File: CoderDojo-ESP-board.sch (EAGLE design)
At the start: 37 parts, among them IC1 ESP-12E/F, IC2 FT232RL, U1 PCA9685PW,118, U2 AMS1117-3.3, X1 PN61729-S

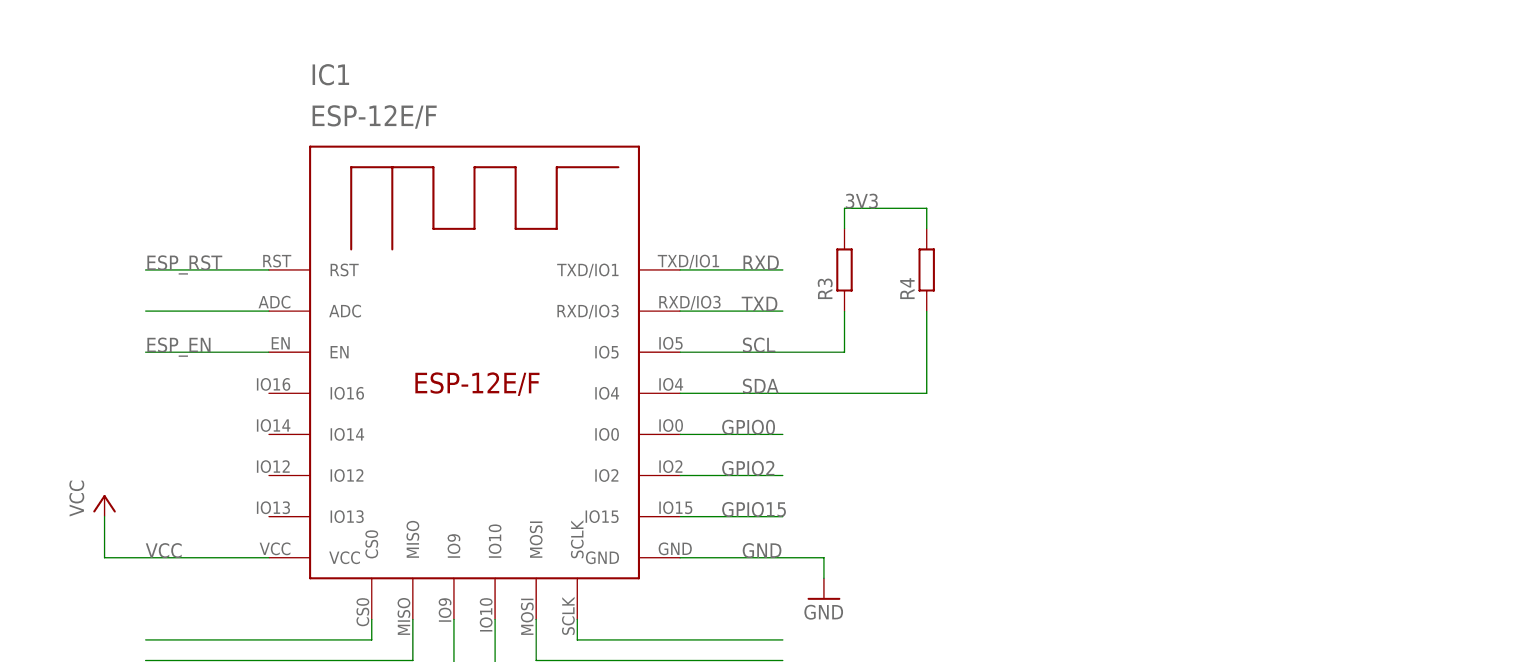
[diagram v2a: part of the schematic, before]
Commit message: add gitignore + add display to schematic
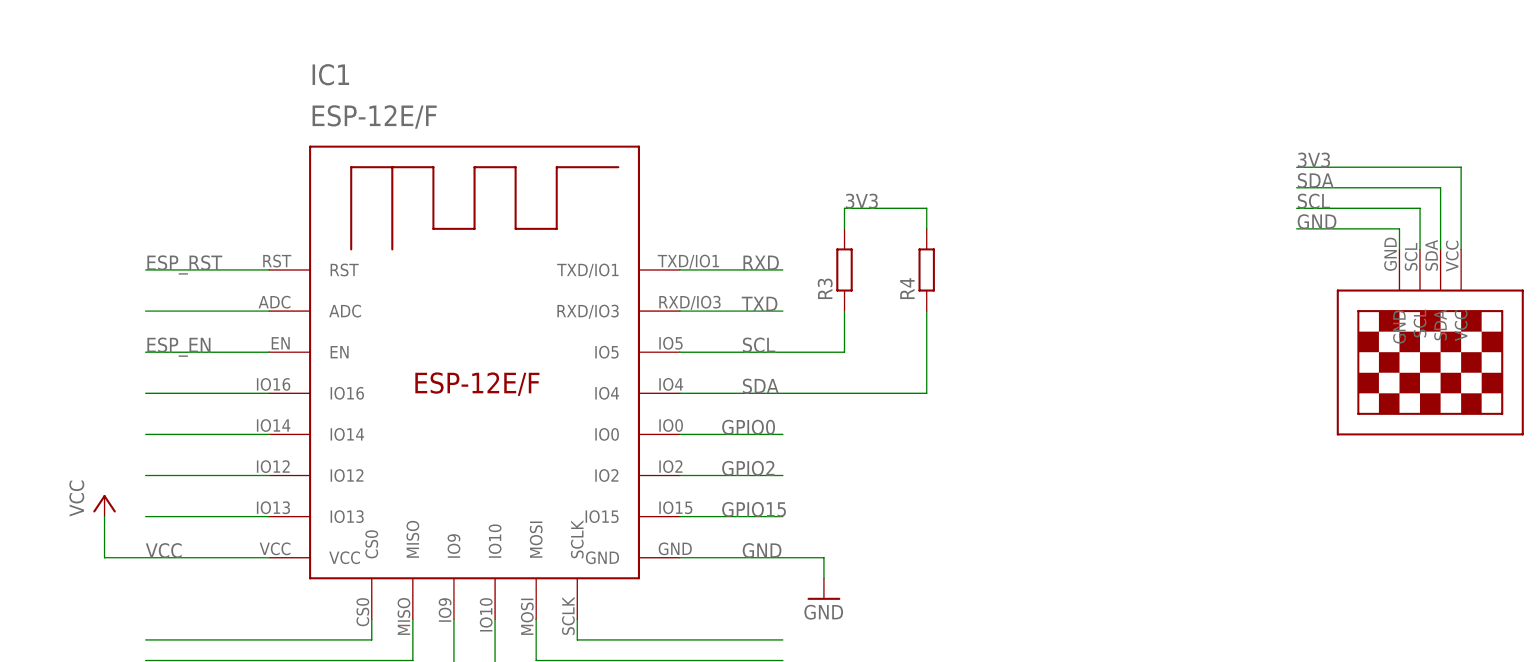
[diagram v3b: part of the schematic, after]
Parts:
- added U$1: 13"OLED13"OLED, 13oled:13"OLED13"OLED
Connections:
- new net N$4: IC1.IO16
- new net N$5: IC1.IO14
- new net N$6: IC1.IO12
- new net N$7: IC1.IO13
- net 3V3: now also U$1.VCC
- net GND: now also U$1.GND
- net SCL: now also U$1.SCL
- net SDA: now also U$1.SDA
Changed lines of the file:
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@@
 <layer number="97" name="Info" color="7" fill="1" visible="yes" active="yes"/>
 <layer number="98" name="Guide" color="6" fill="1" visible="yes" active="yes"/>
+<layer number="101" name="Hidden" color="15" fill="1" visible="yes" active="yes"/>
+<layer number="102" name="Changes" color="12" fill="1" visible="yes" active="yes"/>
 </layers>
 <schematic xreflabel="%F%N/%S.%C%R" xrefpart="/%S.%C%R">
@@
 <part name="C3" library="rcl" library_urn="urn:adsk.eagle:library:334" deviceset="C-EU" device="C0805" package3d_urn="urn:adsk.eagle:package:23617/2"/>
 <part name="C4" library="rcl" library_urn="urn:adsk.eagle:library:334" deviceset="C-EU" device="C0805" package3d_urn="urn:adsk.eagle:package:23617/2"/>
+<part name="U$1" library="13oled" deviceset="13&quot;OLED" device="13&quot;OLED"/>
 </parts>
 <sheets>
@@
 <attribute name="VALUE" x="98.044" y="129.921" size="1.778" layer="96"/>
 </instance>
+<instance part="U$1" gate="G$1" x="314.96" y="71.12" smashed="yes"/>
 </instances>
 <busses>
@@
 <label x="132.08" y="185.42" size="1.778" layer="95"/>
 </segment>
+<segment>
+<pinref part="U$1" gate="G$1" pin="GND"/>
+<wire x1="312.42" y1="83.82" x2="312.42" y2="86.36" width="0.1524" layer="91"/>
+<wire x1="312.42" y1="86.36" x2="299.72" y2="86.36" width="0.1524" layer="91"/>
+<label x="299.72" y="86.36" size="1.778" layer="95"/>
+</segment>
 </net>
 <net name="TXD" class="0">
@@
 <label x="185.42" y="185.42" size="1.778" layer="95"/>
 </segment>
+<segment>
+<pinref part="U$1" gate="G$1" pin="SDA"/>
+<wire x1="317.5" y1="83.82" x2="317.5" y2="91.44" width="0.1524" layer="91"/>
+<wire x1="317.5" y1="91.44" x2="299.72" y2="91.44" width="0.1524" layer="91"/>
+<label x="299.72" y="91.44" size="1.778" layer="95"/>
+</segment>
 </net>
 <net name="SCL" class="0">
@@
 <wire x1="144.78" y1="177.8" x2="132.08" y2="177.8" width="0.1524" layer="91"/>
 <label x="132.08" y="177.8" size="1.778" layer="95"/>
+</segment>
+<segment>
+<pinref part="U$1" gate="G$1" pin="SCL"/>
+<wire x1="314.96" y1="83.82" x2="314.96" y2="88.9" width="0.1524" layer="91"/>
+<wire x1="314.96" y1="88.9" x2="299.72" y2="88.9" width="0.1524" layer="91"/>
+<label x="299.72" y="88.9" size="1.778" layer="95"/>
 </segment>
 </net>
@@
 <label x="86.36" y="142.24" size="1.778" layer="95"/>
 </segment>
+<segment>
+<pinref part="U$1" gate="G$1" pin="VCC"/>
+<wire x1="320.04" y1="83.82" x2="320.04" y2="93.98" width="0.1524" layer="91"/>
+<wire x1="320.04" y1="93.98" x2="299.72" y2="93.98" width="0.1524" layer="91"/>
+<label x="299.72" y="93.98" size="1.778" layer="95"/>
+</segment>
 </net>
 <net name="3V3FT" class="0">
@@
 </segment>
 </net>
+<net name="N$4" class="0">
+<segment>
+<pinref part="IC1" gate="G$1" pin="IO16"/>
+<wire x1="172.72" y1="66.04" x2="157.48" y2="66.04" width="0.1524" layer="91"/>
+</segment>
+</net>
+<net name="N$5" class="0">
+<segment>
+<pinref part="IC1" gate="G$1" pin="IO14"/>
+<wire x1="172.72" y1="60.96" x2="157.48" y2="60.96" width="0.1524" layer="91"/>
+</segment>
+</net>
+<net name="N$6" class="0">
+<segment>
+<pinref part="IC1" gate="G$1" pin="IO12"/>
+<wire x1="172.72" y1="55.88" x2="157.48" y2="55.88" width="0.1524" layer="91"/>
+</segment>
+</net>
+<net name="N$7" class="0">
+<segment>
+<pinref part="IC1" gate="G$1" pin="IO13"/>
+<wire x1="172.72" y1="50.8" x2="157.48" y2="50.8" width="0.1524" layer="91"/>
+</segment>
+</net>

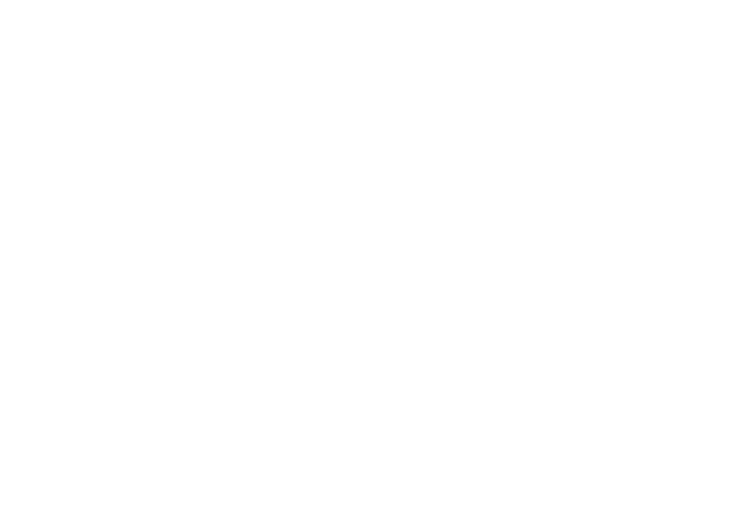
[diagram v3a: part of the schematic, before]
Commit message: Add User buttons
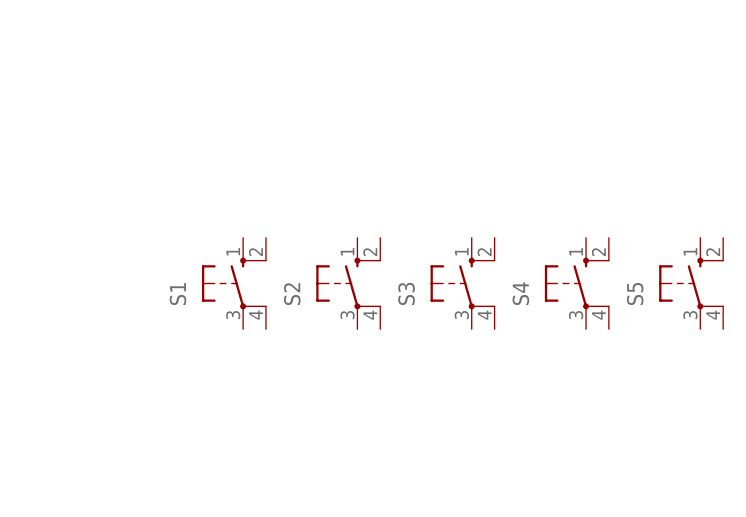
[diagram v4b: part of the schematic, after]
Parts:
- added S1, S2, S3, S4, S5: (no value), switch-omron:10-XX
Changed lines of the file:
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@@
 <part name="C4" library="rcl" library_urn="urn:adsk.eagle:library:334" deviceset="C-EU" device="C0805" package3d_urn="urn:adsk.eagle:package:23617/2"/>
 <part name="U$1" library="13oled" deviceset="13&quot;OLED" device="13&quot;OLED"/>
+<part name="S1" library="switch-omron" library_urn="urn:adsk.eagle:library:377" deviceset="10-XX" device="" package3d_urn="urn:adsk.eagle:package:27496/1"/>
+<part name="S2" library="switch-omron" library_urn="urn:adsk.eagle:library:377" deviceset="10-XX" device="" package3d_urn="urn:adsk.eagle:package:27496/1"/>
+<part name="S3" library="switch-omron" library_urn="urn:adsk.eagle:library:377" deviceset="10-XX" device="" package3d_urn="urn:adsk.eagle:package:27496/1"/>
+<part name="S4" library="switch-omron" library_urn="urn:adsk.eagle:library:377" deviceset="10-XX" device="" package3d_urn="urn:adsk.eagle:package:27496/1"/>
+<part name="S5" library="switch-omron" library_urn="urn:adsk.eagle:library:377" deviceset="10-XX" device="" package3d_urn="urn:adsk.eagle:package:27496/1"/>
 </parts>
 <sheets>
@@
 </instance>
 <instance part="U$1" gate="G$1" x="314.96" y="71.12" smashed="yes"/>
+<instance part="S1" gate="1" x="314.96" y="-7.62" smashed="yes">
+<attribute name="NAME" x="308.61" y="-10.16" size="1.778" layer="95" rot="R90"/>
+<attribute name="VALUE" x="311.15" y="-4.445" size="1.778" layer="96" rot="R90"/>
+</instance>
+<instance part="S2" gate="1" x="327.66" y="-7.62" smashed="yes">
+<attribute name="NAME" x="321.31" y="-10.16" size="1.778" layer="95" rot="R90"/>
+<attribute name="VALUE" x="323.85" y="-4.445" size="1.778" layer="96" rot="R90"/>
+</instance>
+<instance part="S3" gate="1" x="340.36" y="-7.62" smashed="yes">
+<attribute name="NAME" x="334.01" y="-10.16" size="1.778" layer="95" rot="R90"/>
+<attribute name="VALUE" x="336.55" y="-4.445" size="1.778" layer="96" rot="R90"/>
+</instance>
+<instance part="S4" gate="1" x="353.06" y="-7.62" smashed="yes">
+<attribute name="NAME" x="346.71" y="-10.16" size="1.778" layer="95" rot="R90"/>
+<attribute name="VALUE" x="349.25" y="-4.445" size="1.778" layer="96" rot="R90"/>
+</instance>
+<instance part="S5" gate="1" x="365.76" y="-7.62" smashed="yes">
+<attribute name="NAME" x="359.41" y="-10.16" size="1.778" layer="95" rot="R90"/>
+<attribute name="VALUE" x="361.95" y="-4.445" size="1.778" layer="96" rot="R90"/>
+</instance>
 </instances>
 <busses>

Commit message: update
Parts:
- added R18, R19, R20, R21, R22: 12K, rcl:R-EU_R0805
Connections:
- removed net N$35: C3.1, U2.VIN
- new net BTN_C: R19.2, S2.P
- new net BTN_D: R20.2, S3.P
- new net BTN_L: R21.2, S4.P
- new net BTN_R: R22.2, S5.P
- new net BTN_U: R18.2, S1.P
- net 3V3: now also S1.S, S2.S, S3.S, S4.S, S5.S
- net 5VUSB: now also C3.1, U2.VIN
- net GND: now also R18.1, R19.1, R20.1, R21.1, R22.1
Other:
- moved on the sheet: C1, C2, C3, C4, IC1, IC2, JP1, LED0, LED1, LED2, LED3, LED4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

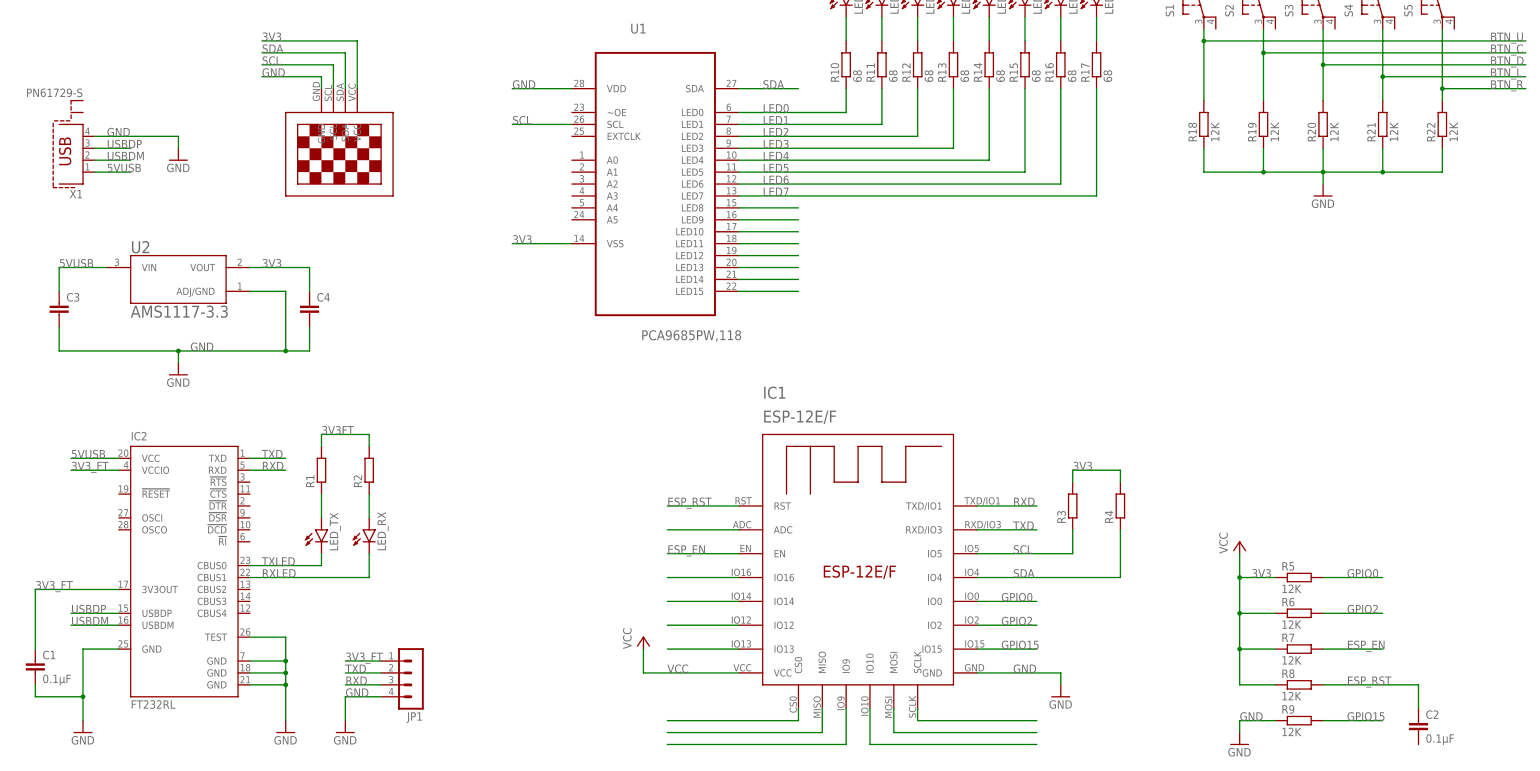
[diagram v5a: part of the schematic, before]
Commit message: Add L293D Motor driver
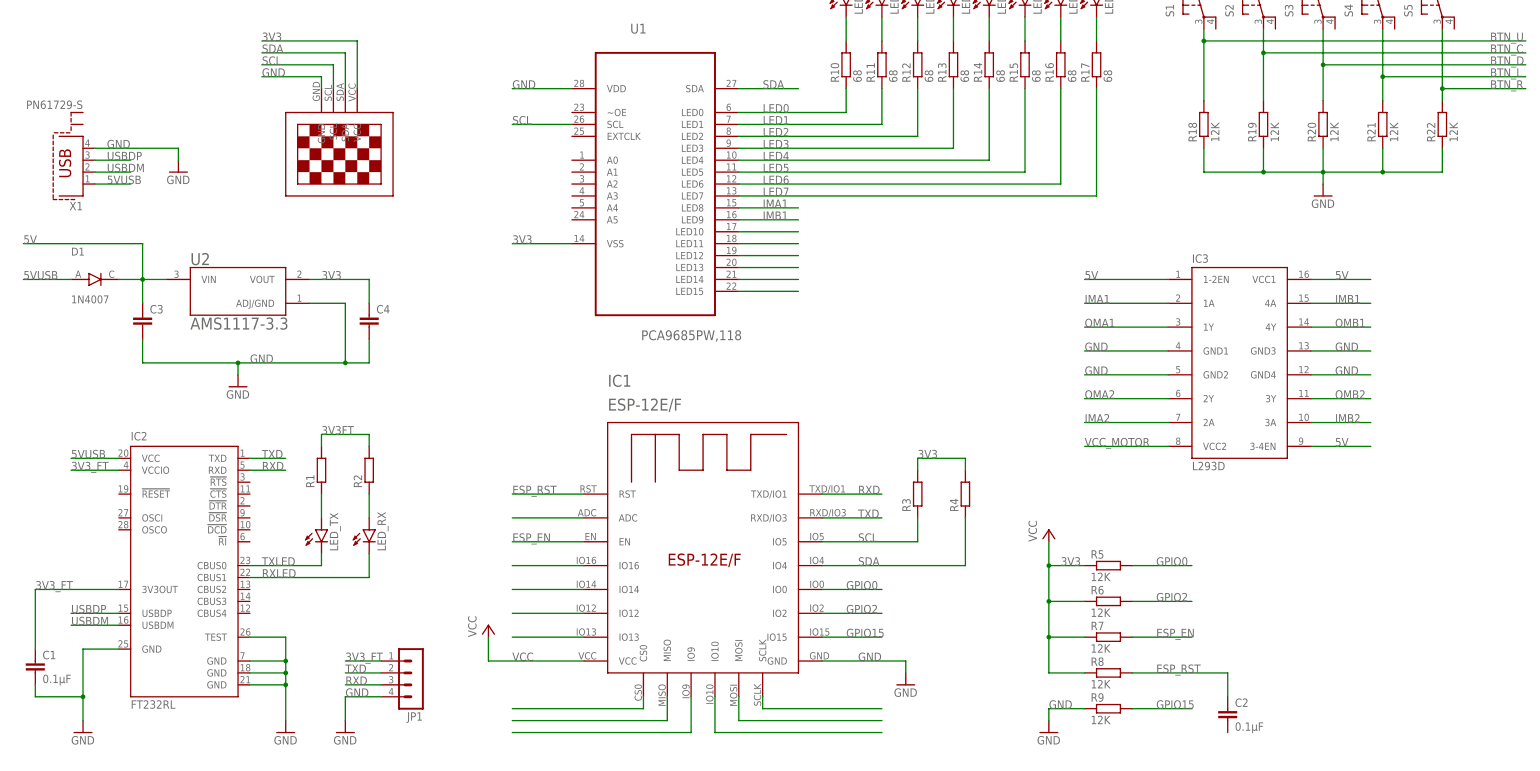
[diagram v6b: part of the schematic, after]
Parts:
- added D1: 1N4007, 1N4007:1N4007
- added IC3: L293D, st-microelectronics:L293D
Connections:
- removed net N$19: U1.LED8
- removed net N$20: U1.LED9
- new net 5V: C3.1, D1.C, IC3.1-2EN, IC3.3-4EN, IC3.VCC1, U2.VIN
- new net IMA1: IC3.1A, U1.LED8
- new net IMA2: IC3.2A
- new net IMB1: IC3.4A, U1.LED9
- new net IMB2: IC3.3A
- new net OMA1: IC3.1Y
- new net OMA2: IC3.2Y
- new net OMB1: IC3.4Y
- new net OMB2: IC3.3Y
- new net VCC_MOTOR: IC3.VCC2
- net 5VUSB: now also D1.A; no longer C3.1, U2.VIN
- net GND: now also IC3.GND1, IC3.GND2, IC3.GND3, IC3.GND4
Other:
- moved on the sheet: C2, C3, C4, IC1, R3, R4, R5, R6, R7, R8, R9, U2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
